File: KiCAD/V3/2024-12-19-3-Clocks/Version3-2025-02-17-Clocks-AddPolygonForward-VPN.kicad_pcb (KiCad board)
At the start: 2 copper layers, 90 x 85 mm, 9 parts, among them J1 Conn_01x04_Pin, J2 Conn_01x04_Pin, J3 Conn_01x04_Pin, SW1 SW_DIP_x01

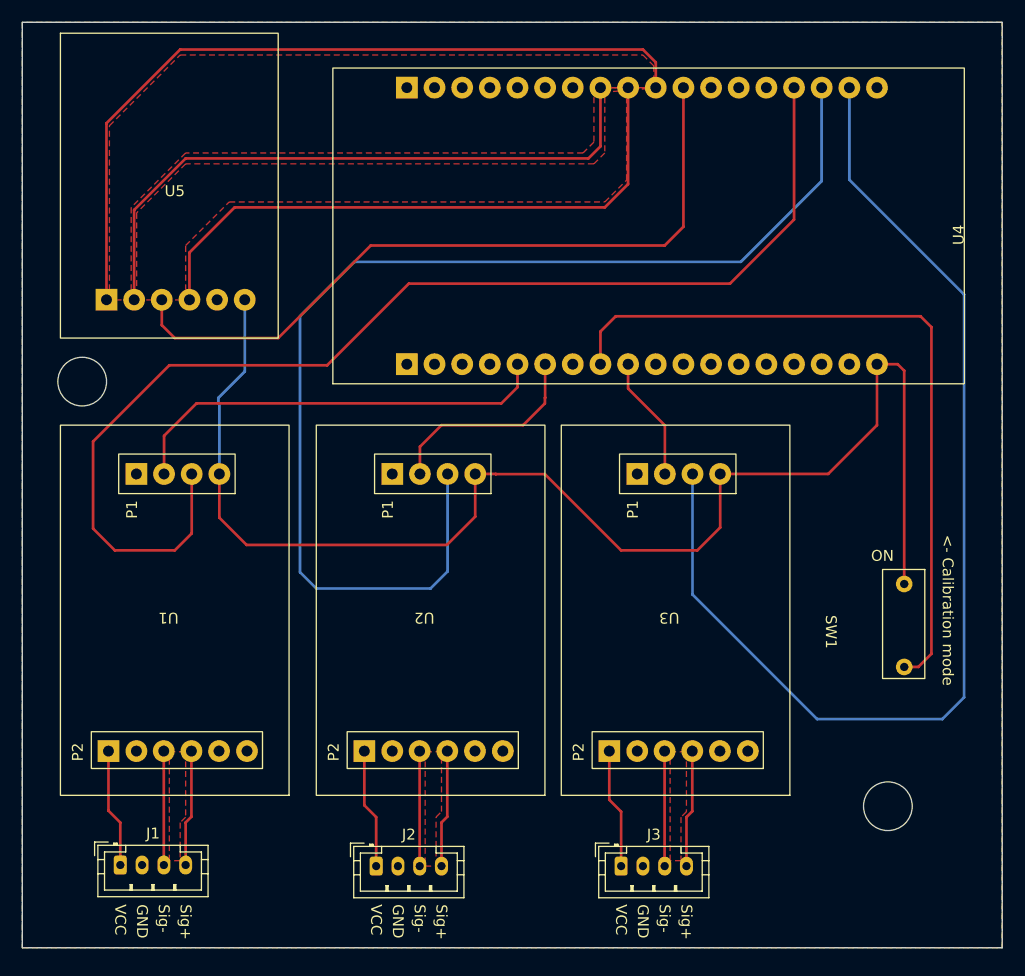
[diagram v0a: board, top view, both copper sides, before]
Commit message: Faire version 3 de PCB
Avec polygone aux deux layers.
Avec une clock par controllers.
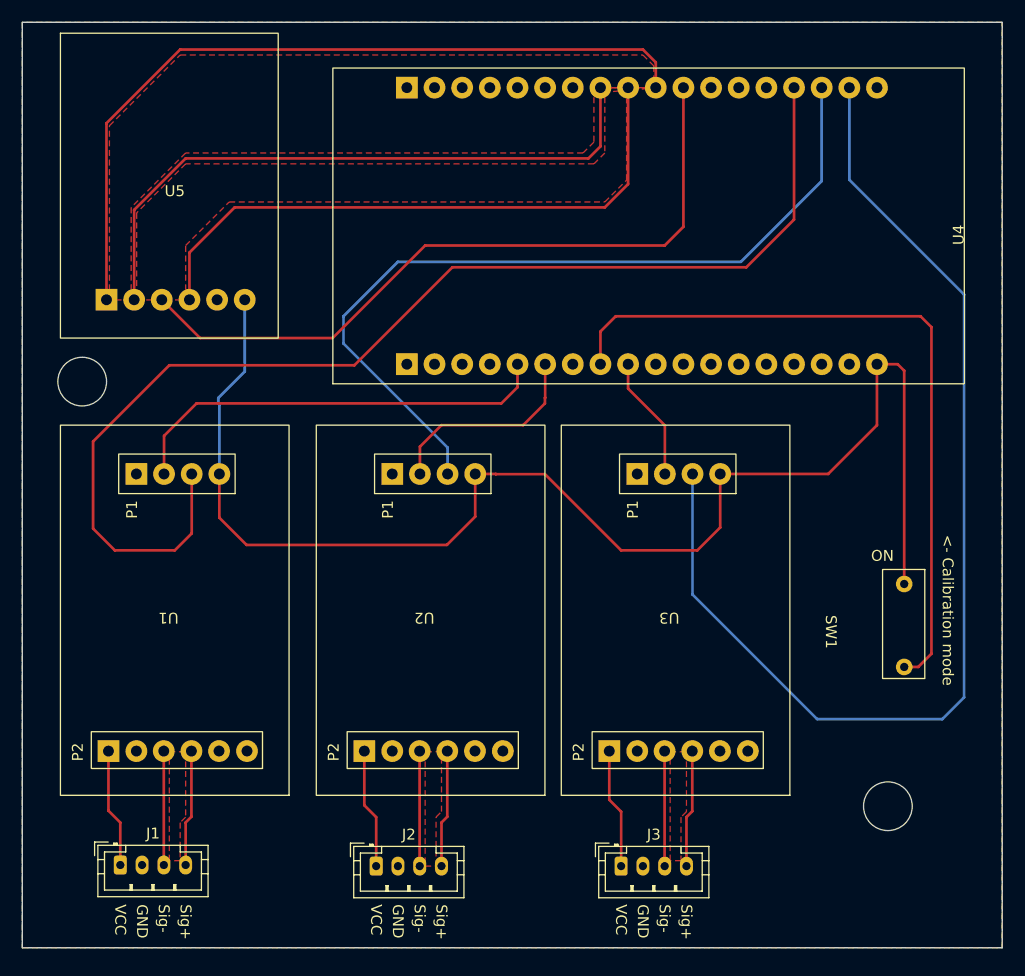
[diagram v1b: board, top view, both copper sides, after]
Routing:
- net Net-(U2-SCK): track 108.9 -> 76.1 mm
- net Net-(U4-SDA/IO21): track 67.7 -> 66.4 mm
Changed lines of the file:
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@@
 			(drillshape 0)
 			(scaleselection 1)
-			(outputdirectory "GerberFiles-Version3-20250217/")
+			(outputdirectory "GerberFiles-Version2-20240612/")
 		)
 	)
@@
 	)
 	(segment
-		(start 104 85)
-		(end 133.5 85)
+		(start 82 92.5)
+		(end 99 92.5)
 		(width 0.25)
 		(layer "F.Cu")
@@
 	)
 	(segment
-		(start 75 107.5)
-		(end 75 99.5)
+		(start 84.0574 102.4834)
+		(end 84.0574 107.9426)
 		(width 0.25)
 		(layer "F.Cu")
@@
 	)
 	(segment
-		(start 84.0574 102.4834)
-		(end 84.0574 107.9426)
+		(start 82.5 109.5)
+		(end 77 109.5)
 		(width 0.25)
 		(layer "F.Cu")
@@
 	)
 	(segment
-		(start 82 92.5)
-		(end 96.5 92.5)
+		(start 135 83.5)
+		(end 139.38 79.12)
 		(width 0.25)
 		(layer "F.Cu")
@@
 	)
 	(segment
-		(start 139.38 79.12)
-		(end 139.38 67)
+		(start 75 107.5)
+		(end 75 99.5)
 		(width 0.25)
 		(layer "F.Cu")
@@
 	)
 	(segment
-		(start 133.5 85)
-		(end 139.38 79.12)
+		(start 139.38 79.12)
+		(end 139.38 67)
 		(width 0.25)
 		(layer "F.Cu")
@@
 	)
 	(segment
-		(start 82.5 109.5)
-		(end 77 109.5)
+		(start 84.0574 107.9426)
+		(end 82.5 109.5)
 		(width 0.25)
 		(layer "F.Cu")
@@
 	)
 	(segment
-		(start 96.5 92.5)
-		(end 104 85)
+		(start 75 99.5)
+		(end 82 92.5)
 		(width 0.25)
 		(layer "F.Cu")
@@
 	)
 	(segment
-		(start 84.0574 107.9426)
-		(end 82.5 109.5)
+		(start 99 92.5)
+		(end 108 83.5)
 		(width 0.25)
 		(layer "F.Cu")
@@
 	)
 	(segment
-		(start 75 99.5)
-		(end 82 92.5)
+		(start 108 83.5)
+		(end 135 83.5)
 		(width 0.25)
 		(layer "F.Cu")
@@
 	)
 	(segment
-		(start 129.22 67)
-		(end 129.22 79.78)
+		(start 105.5 81.5)
+		(end 97 90)
 		(width 0.25)
 		(layer "F.Cu")
@@
 	)
 	(segment
-		(start 92 90)
-		(end 82.5 90)
+		(start 127.5 81.5)
+		(end 105.5 81.5)
 		(width 0.25)
 		(layer "F.Cu")
@@
 	)
 	(segment
-		(start 127.5 81.5)
-		(end 100.5 81.5)
+		(start 84.8266 90)
+		(end 81.3102 86.4836)
 		(width 0.25)
 		(layer "F.Cu")
@@
 	)
 	(segment
-		(start 82.5 90)
-		(end 81.3102 88.8102)
+		(start 97 90)
+		(end 84.8266 90)
 		(width 0.25)
 		(layer "F.Cu")
@@
 	)
 	(segment
-		(start 100.5 81.5)
-		(end 92 90)
-		(width 0.25)
-		(layer "F.Cu")
-		(net 32)
-	)
-	(segment
-		(start 81.3102 88.8102)
-		(end 81.3102 86.4836)
+		(start 129.22 67)
+		(end 129.22 79.78)
 		(width 0.25)
 		(layer "F.Cu")
@@
 	)
 	(segment
-		(start 94 88)
-		(end 99 83)
-		(width 0.25)
-		(layer "B.Cu")
-		(net 39)
-	)
-	(segment
-		(start 95.5 113)
-		(end 94 111.5)
-		(width 0.25)
-		(layer "B.Cu")
-		(net 39)
-	)
-	(segment
-		(start 94 111.5)
-		(end 94 88)
+		(start 98 90.5)
+		(end 107.5574 100.0574)
 		(width 0.25)
 		(layer "B.Cu")
@@
 	)
 	(segment
-		(start 134.5 83)
+		(start 141.92 67)
 		(end 141.92 75.58)
 		(width 0.25)
@@
 	)
 	(segment
-		(start 107.5574 102.4834)
-		(end 107.5574 111.4426)
+		(start 141.92 75.58)
+		(end 134.5 83)
 		(width 0.25)
 		(layer "B.Cu")
@@
 	)
 	(segment
-		(start 141.92 75.58)
-		(end 141.92 67)
+		(start 107.5574 100.0574)
+		(end 107.5574 102.4834)
 		(width 0.25)
 		(layer "B.Cu")
@@
 	)
 	(segment
-		(start 107.5574 111.4426)
-		(end 106 113)
+		(start 134.5 83)
+		(end 103 83)
 		(width 0.25)
 		(layer "B.Cu")
@@
 	)
 	(segment
-		(start 106 113)
-		(end 95.5 113)
+		(start 103 83)
+		(end 98 88)
 		(width 0.25)
 		(layer "B.Cu")
@@
 	)
 	(segment
-		(start 99 83)
-		(end 134.5 83)
+		(start 98 88)
+		(end 98 90.5)
 		(width 0.25)
 		(layer "B.Cu")
